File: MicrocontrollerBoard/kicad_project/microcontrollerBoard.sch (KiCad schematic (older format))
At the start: 48 parts, among them J1 PROG_CONN, J10 PC_5V, J13 PA_GND, J14 PB_GND, J15 PC_GND, J18 COM, J19 COM_5V, J2 5V_CONN, J20 COM_GND, J21 POWER_CONN, J22 MOTOR2, J23 MOTOR1, J3 PA, J4 PB, J5 PC, J6 3V_CONN_1, J7 3V_CONN_2, J8 PA_5V, J9 PB_5V, U1 ATmega1284P-PU, U2 TC4422, U3 TC4422, U4 TC4422, U5 TC4422, U6 AMS1117-3.3, Y1 16MHz

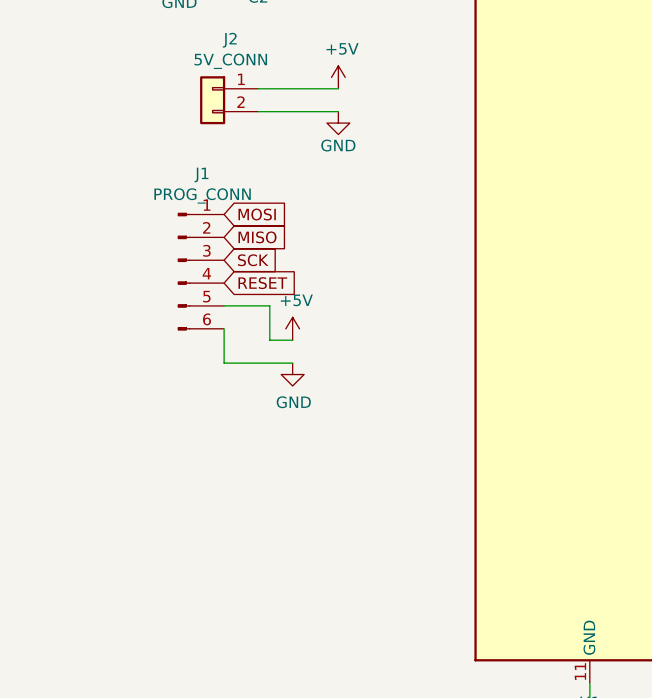
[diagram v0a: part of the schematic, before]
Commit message: uC board: Added resistors to MISO, brought out a RESET pin, minor fixes.
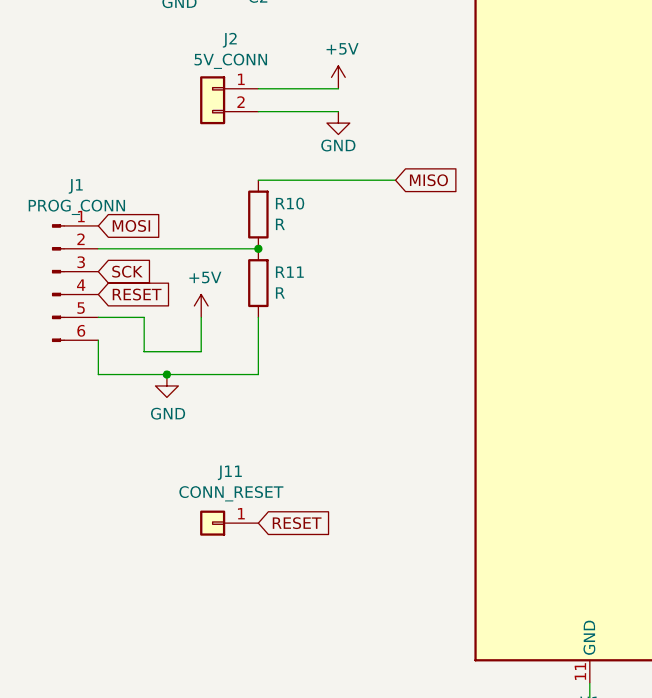
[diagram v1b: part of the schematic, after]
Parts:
- added J11: CONN_RESET, Connector_PinHeader_2.54mm:PinHeader_1x01_P2.54mm_Vertical, symbol Connector_Generic:Conn_01x01
- added R10, R11: R, Resistor_SMD:R_0805_2012Metric_Pad1.15x1.40mm_HandSolder, symbol Device:R
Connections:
- net GND: now also R11.1
- net MISO: now also R10.2; no longer J1.2 (Pin_2)
- net RESET: now also J11.1 (Pin_1)
- new net: J1.2 (Pin_2), R10.1, R11.2
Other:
- moved on the sheet: J1
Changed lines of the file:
@@
 L Connector:Conn_01x06_Male J1
 U 1 1 5BC7F9DC
-P 1500 3650
-F 0 "J1" H 1606 4028 50  0000 C CNN
-F 1 "PROG_CONN" H 1606 3937 50  0000 C CNN
-F 2 "Connector_PinHeader_2.54mm:PinHeader_1x06_P2.54mm_Vertical" H 1500 3650 50  0001 C CNN
-F 3 "~" H 1500 3650 50  0001 C CNN
-	1    1500 3650
+P 950 3700
+F 0 "J1" H 1056 4078 50  0000 C CNN
+F 1 "PROG_CONN" H 1056 3987 50  0000 C CNN
+F 2 "Connector_PinHeader_2.54mm:PinHeader_1x06_P2.54mm_Vertical" H 950 3700 50  0001 C CNN
+F 3 "~" H 950 3700 50  0001 C CNN
+	1    950  3700
 	1    0    0    -1
 $EndComp
@@
 L power:GND #PWR03
 U 1 1 5BC7FD8A
-P 2000 4100
-F 0 "#PWR03" H 2000 3850 50  0001 C CNN
-F 1 "GND" H 2005 3927 50  0000 C CNN
-F 2 "" H 2000 4100 50  0001 C CNN
-F 3 "" H 2000 4100 50  0001 C CNN
-	1    2000 4100
+P 1450 4150
+F 0 "#PWR03" H 1450 3900 50  0001 C CNN
+F 1 "GND" H 1455 3977 50  0000 C CNN
+F 2 "" H 1450 4150 50  0001 C CNN
+F 3 "" H 1450 4150 50  0001 C CNN
+	1    1450 4150
 	1    0    0    -1
 $EndComp
@@
 L power:+5V #PWR02
 U 1 1 5BC7FDAD
-P 2000 4000
-F 0 "#PWR02" H 2000 3850 50  0001 C CNN
-F 1 "+5V" H 2015 4173 50  0000 C CNN
-F 2 "" H 2000 4000 50  0001 C CNN
-F 3 "" H 2000 4000 50  0001 C CNN
-	1    2000 4000
-	1    0    0    -1
-$EndComp
-Text GLabel 1700 3750 2    50   Input ~ 0
+P 1600 3900
+F 0 "#PWR02" H 1600 3750 50  0001 C CNN
+F 1 "+5V" H 1615 4073 50  0000 C CNN
+F 2 "" H 1600 3900 50  0001 C CNN
+F 3 "" H 1600 3900 50  0001 C CNN
+	1    1600 3900
+	1    0    0    -1
+$EndComp
+Text GLabel 1150 3800 2    50   Input ~ 0
 RESET
-Text GLabel 1700 3650 2    50   Input ~ 0
+Text GLabel 1150 3700 2    50   Input ~ 0
 SCK
-Text GLabel 1700 3550 2    50   Input ~ 0
+Text GLabel 2450 3300 2    50   Input ~ 0
 MISO
-Text GLabel 1700 3450 2    50   Input ~ 0
+Text GLabel 1150 3500 2    50   Input ~ 0
 MOSI
 Wire Wire Line
-	1700 3850 1900 3850
-Wire Wire Line
-	1900 3850 1900 4000
-Wire Wire Line
-	1900 4000 2000 4000
-Wire Wire Line
-	1700 3950 1700 4100
-Wire Wire Line
-	1700 4100 2000 4100
+	1150 3900 1350 3900
+Wire Wire Line
+	1350 3900 1350 4050
+Wire Wire Line
+	1150 4000 1150 4150
+Wire Wire Line
+	1150 4150 1450 4150
 $Comp
 L Device:LED D1
@@
 	5800 6600 6300 6600
 Connection ~ 5800 6600
+$Comp
+L Connector_Generic:Conn_01x01 J11
+U 1 1 5BE3FF3A
+P 1650 4800
+F 0 "J11" H 1570 4575 50  0000 C CNN
+F 1 "CONN_RESET" H 1570 4666 50  0000 C CNN
+F 2 "Connector_PinHeader_2.54mm:PinHeader_1x01_P2.54mm_Vertical" H 1650 4800 50  0001 C CNN
+F 3 "~" H 1650 4800 50  0001 C CNN
+	1    1650 4800
+	-1   0    0    1
+$EndComp
+Text GLabel 1850 4800 2    50   Input ~ 0
+RESET
+$Comp
+L Device:R R10
+U 1 1 5BE4ABDC
+P 1850 3450
+F 0 "R10" H 1780 3404 50  0000 R CNN
+F 1 "R" H 1780 3495 50  0000 R CNN
+F 2 "Resistor_SMD:R_0805_2012Metric_Pad1.15x1.40mm_HandSolder" V 1780 3450 50  0001 C CNN
+F 3 "~" H 1850 3450 50  0001 C CNN
+	1    1850 3450
+	-1   0    0    1
+$EndComp
+$Comp
+L Device:R R11
+U 1 1 5BE4AE93
+P 1850 3750
+F 0 "R11" H 1780 3704 50  0000 R CNN
+F 1 "R" H 1780 3795 50  0000 R CNN
+F 2 "Resistor_SMD:R_0805_2012Metric_Pad1.15x1.40mm_HandSolder" V 1780 3750 50  0001 C CNN
+F 3 "~" H 1850 3750 50  0001 C CNN
+	1    1850 3750
+	-1   0    0    1
+$EndComp
+Wire Wire Line
+	1850 3600 1150 3600
+Connection ~ 1850 3600
+Wire Wire Line
+	1850 3900 1850 4150
+Wire Wire Line
+	1850 4150 1450 4150
+Connection ~ 1450 4150
+Wire Wire Line
+	1850 3300 2450 3300
+Wire Wire Line
+	1350 4050 1600 4050
+Wire Wire Line
+	1600 4050 1600 3900
 $EndSCHEMATC

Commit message: uC board: V_IN is no longer exposed. Better power routing.
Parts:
- J13, J3, J8: footprint Connector_PinHeader_2.54mm:PinHeader_1x08_P2.54mm_Vertical -> Connector_PinHeader_2.54mm:PinHeader_1x07_P2.54mm_Vertical; symbol Connector_Generic:Conn_01x08 -> Connector_Generic:Conn_01x07
- R10: value R -> 1K
- R11: value R -> 2K
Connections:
- net +5V: no longer J8.8 (Pin_8)
- net +BATT: now also R3.1
- net GND: no longer J13.8 (Pin_8)
- net at U1.33 (PA7): now also J3.7 (Pin_7); no longer J3.8 (Pin_8)
- net at U1.34 (PA6): now also J3.6 (Pin_6); no longer J3.7 (Pin_7)
- net at U1.35 (PA5): now also J3.5 (Pin_5); no longer J3.6 (Pin_6)
- net at U1.36 (PA4): now also J3.4 (Pin_4); no longer J3.5 (Pin_5)
- net at U1.37 (PA3): now also J3.3 (Pin_3); no longer J3.4 (Pin_4)
- net at U1.38 (PA2): now also J3.2 (Pin_2); no longer J3.3 (Pin_3)
- net at U1.39 (PA1): now also J3.1 (Pin_1); no longer J3.2 (Pin_2)
- removed net V_EXT: J3.1 (Pin_1), R3.1
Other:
- note added: "V_IN = V_BAT * R4 / ( R3 + R4)\n\nKeep V_IN < 5V with a safe margin!"
- note removed: "V_IN = V_EXT * RB / ( RA + RB)"
- moved on the sheet: R3, R4
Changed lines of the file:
@@
 L Device:R R3
 U 1 1 5BCE0BEC
-P 7150 1750
-F 0 "R3" H 7220 1796 50  0000 L CNN
-F 1 "RA" H 7220 1705 50  0000 L CNN
-F 2 "Resistor_SMD:R_0805_2012Metric_Pad1.15x1.40mm_HandSolder" V 7080 1750 50  0001 C CNN
-F 3 "~" H 7150 1750 50  0001 C CNN
-	1    7150 1750
+P 7000 2000
+F 0 "R3" H 7070 2046 50  0000 L CNN
+F 1 "RA" H 7070 1955 50  0000 L CNN
+F 2 "Resistor_SMD:R_0805_2012Metric_Pad1.15x1.40mm_HandSolder" V 6930 2000 50  0001 C CNN
+F 3 "~" H 7000 2000 50  0001 C CNN
+	1    7000 2000
 	1    0    0    -1
 $EndComp
@@
 L Device:R R4
 U 1 1 5BCE0BF2
-P 7150 2050
-F 0 "R4" H 7220 2096 50  0000 L CNN
-F 1 "RB" H 7220 2005 50  0000 L CNN
-F 2 "Resistor_SMD:R_0805_2012Metric_Pad1.15x1.40mm_HandSolder" V 7080 2050 50  0001 C CNN
-F 3 "~" H 7150 2050 50  0001 C CNN
-	1    7150 2050
+P 7000 2300
+F 0 "R4" H 7070 2346 50  0000 L CNN
+F 1 "RB" H 7070 2255 50  0000 L CNN
+F 2 "Resistor_SMD:R_0805_2012Metric_Pad1.15x1.40mm_HandSolder" V 6930 2300 50  0001 C CNN
+F 3 "~" H 7000 2300 50  0001 C CNN
+	1    7000 2300
 	1    0    0    -1
 $EndComp
@@
 L power:GND #PWR015
 U 1 1 5BCE0BF8
-P 7150 2200
-F 0 "#PWR015" H 7150 1950 50  0001 C CNN
-F 1 "GND" H 7155 2027 50  0000 C CNN
-F 2 "" H 7150 2200 50  0001 C CNN
-F 3 "" H 7150 2200 50  0001 C CNN
-	1    7150 2200
-	1    0    0    -1
-$EndComp
-Text GLabel 7450 1600 2    50   Input ~ 0
-V_EXT
-Wire Wire Line
-	7150 1600 7450 1600
-Wire Wire Line
-	7150 1900 6850 1900
-Connection ~ 7150 1900
-Text GLabel 6850 1900 0    50   Input ~ 0
+P 7000 2450
+F 0 "#PWR015" H 7000 2200 50  0001 C CNN
+F 1 "GND" H 7005 2277 50  0000 C CNN
+F 2 "" H 7000 2450 50  0001 C CNN
+F 3 "" H 7000 2450 50  0001 C CNN
+	1    7000 2450
+	1    0    0    -1
+$EndComp
+Wire Wire Line
+	7000 1850 7300 1850
+Wire Wire Line
+	7000 2150 6700 2150
+Connection ~ 7000 2150
+Text GLabel 6700 2150 0    50   Input ~ 0
 V_IN
-Text GLabel 3900 1800 2    50   Input ~ 0
-V_IN
-Text Notes 6600 2500 0    50   ~ 0
-V_IN = V_EXT * RB / ( RA + RB)
+Text Notes 6450 3000 0    50   ~ 0
+  V_IN = V_BAT * R4 / ( R3 + R4)\n\nKeep V_IN < 5V with a safe margin!
 $Comp
 L Connector_Generic:Conn_01x04 J9
@@
 $EndComp
 $Comp
-L Connector_Generic:Conn_01x08 J3
+L Connector_Generic:Conn_01x07 J3
 U 1 1 5BD3F1C1
-P 4800 2100
-F 0 "J3" H 4750 2600 50  0000 L CNN
-F 1 "PA" H 4750 2500 50  0000 L CNN
-F 2 "Connector_PinHeader_2.54mm:PinHeader_1x08_P2.54mm_Vertical" H 4800 2100 50  0001 C CNN
-F 3 "~" H 4800 2100 50  0001 C CNN
-	1    4800 2100
+P 4800 2200
+F 0 "J3" H 4750 2700 50  0000 L CNN
+F 1 "PA" H 4750 2600 50  0000 L CNN
+F 2 "Connector_PinHeader_2.54mm:PinHeader_1x07_P2.54mm_Vertical" H 4800 2200 50  0001 C CNN
+F 3 "~" H 4800 2200 50  0001 C CNN
+	1    4800 2200
 	1    0    0    -1
 $EndComp
@@
 Wire Wire Line
 	4600 1900 3900 1900
-Text GLabel 4600 1800 0    50   Input ~ 0
-V_EXT
-$Comp
-L Connector_Generic:Conn_01x08 J8
+$Comp
+L Connector_Generic:Conn_01x07 J8
 U 1 1 5BD6F2E7
-P 5350 2100
-F 0 "J8" H 5300 2600 50  0000 L CNN
-F 1 "PA_5V" H 5300 2500 50  0000 L CNN
-F 2 "Connector_PinHeader_2.54mm:PinHeader_1x08_P2.54mm_Vertical" H 5350 2100 50  0001 C CNN
-F 3 "~" H 5350 2100 50  0001 C CNN
-	1    5350 2100
-	1    0    0    -1
-$EndComp
-$Comp
-L Connector_Generic:Conn_01x08 J13
+P 5350 2200
+F 0 "J8" H 5300 2700 50  0000 L CNN
+F 1 "PA_5V" H 5300 2600 50  0000 L CNN
+F 2 "Connector_PinHeader_2.54mm:PinHeader_1x07_P2.54mm_Vertical" H 5350 2200 50  0001 C CNN
+F 3 "~" H 5350 2200 50  0001 C CNN
+	1    5350 2200
+	1    0    0    -1
+$EndComp
+$Comp
+L Connector_Generic:Conn_01x07 J13
 U 1 1 5BD6F3CA
-P 5900 2100
-F 0 "J13" H 5850 2600 50  0000 L CNN
-F 1 "PA_GND" H 5850 2500 50  0000 L CNN
-F 2 "Connector_PinHeader_2.54mm:PinHeader_1x08_P2.54mm_Vertical" H 5900 2100 50  0001 C CNN
-F 3 "~" H 5900 2100 50  0001 C CNN
-	1    5900 2100
-	1    0    0    -1
-$EndComp
-Wire Wire Line
-	5150 2800 5150 2500
-Wire Wire Line
-	5150 2500 5150 2400
-Connection ~ 5150 2500
-Wire Wire Line
-	5150 2400 5150 2300
-Connection ~ 5150 2400
-Wire Wire Line
-	5150 2300 5150 2200
-Connection ~ 5150 2300
-Wire Wire Line
-	5150 2200 5150 2100
-Connection ~ 5150 2200
-Wire Wire Line
-	5150 2100 5150 2000
-Connection ~ 5150 2100
-Wire Wire Line
-	5150 2000 5150 1900
-Connection ~ 5150 2000
-Wire Wire Line
-	5150 1900 5150 1800
-Connection ~ 5150 1900
-Wire Wire Line
-	5700 2800 5700 2500
+P 5900 2200
+F 0 "J13" H 5850 2700 50  0000 L CNN
+F 1 "PA_GND" H 5850 2600 50  0000 L CNN
+F 2 "Connector_PinHeader_2.54mm:PinHeader_1x07_P2.54mm_Vertical" H 5900 2200 50  0001 C CNN
+F 3 "~" H 5900 2200 50  0001 C CNN
+	1    5900 2200
+	1    0    0    -1
+$EndComp
 Connection ~ 5700 2800
-Wire Wire Line
-	5700 2500 5700 2400
-Connection ~ 5700 2500
-Wire Wire Line
-	5700 2400 5700 2300
-Connection ~ 5700 2400
-Wire Wire Line
-	5700 2300 5700 2200
-Connection ~ 5700 2300
-Wire Wire Line
-	5700 2200 5700 2100
-Connection ~ 5700 2200
-Wire Wire Line
-	5700 2100 5700 2000
-Connection ~ 5700 2100
-Wire Wire Line
-	5700 2000 5700 1900
-Connection ~ 5700 2000
-Wire Wire Line
-	5700 1900 5700 1800
-Connection ~ 5700 1900
 $Comp
 L Connector_Generic:Conn_01x04 J18
@@
 	1    0    0    -1
 $EndComp
-Wire Wire Line
-	5150 1650 5150 1800
-Connection ~ 5150 1800
 $Comp
 L Connector_Generic:Conn_01x08 J15
@@
 P 1850 3450
 F 0 "R10" H 1780 3404 50  0000 R CNN
-F 1 "R" H 1780 3495 50  0000 R CNN
+F 1 "1K" H 1780 3495 50  0000 R CNN
 F 2 "Resistor_SMD:R_0805_2012Metric_Pad1.15x1.40mm_HandSolder" V 1780 3450 50  0001 C CNN
 F 3 "~" H 1850 3450 50  0001 C CNN
@@
 P 1850 3750
 F 0 "R11" H 1780 3704 50  0000 R CNN
-F 1 "R" H 1780 3795 50  0000 R CNN
+F 1 "2K" H 1780 3795 50  0000 R CNN
 F 2 "Resistor_SMD:R_0805_2012Metric_Pad1.15x1.40mm_HandSolder" V 1780 3750 50  0001 C CNN
 F 3 "~" H 1850 3750 50  0001 C CNN
@@
 Wire Wire Line
 	1600 4050 1600 3900
+Connection ~ 5150 1900
+Connection ~ 5150 2000
+Connection ~ 5150 2100
+Connection ~ 5150 2200
+Connection ~ 5150 2300
+Connection ~ 5150 2400
+Connection ~ 5150 2500
+Wire Wire Line
+	5150 2500 5150 2800
+Wire Wire Line
+	5150 2400 5150 2500
+Wire Wire Line
+	5150 1650 5150 1900
+Wire Wire Line
+	5150 2300 5150 2400
+Wire Wire Line
+	5150 2200 5150 2300
+Wire Wire Line
+	5150 2100 5150 2200
+Wire Wire Line
+	5150 2000 5150 2100
+Wire Wire Line
+	5150 1900 5150 2000
+Wire Wire Line
+	5700 1900 5700 2000
+Wire Wire Line
+	5700 2000 5700 2100
+Connection ~ 5700 2000
+Wire Wire Line
+	5700 2100 5700 2200
+Connection ~ 5700 2100
+Wire Wire Line
+	5700 2200 5700 2300
+Connection ~ 5700 2200
+Wire Wire Line
+	5700 2300 5700 2400
+Connection ~ 5700 2300
+Wire Wire Line
+	5700 2400 5700 2500
+Connection ~ 5700 2400
+Wire Wire Line
+	5700 2500 5700 2800
+Connection ~ 5700 2500
+$Comp
+L power:+BATT #PWR0101
+U 1 1 5BEFB538
+P 7300 1850
+F 0 "#PWR0101" H 7300 1700 50  0001 C CNN
+F 1 "+BATT" H 7315 2023 50  0000 C CNN
+F 2 "" H 7300 1850 50  0001 C CNN
+F 3 "" H 7300 1850 50  0001 C CNN
+	1    7300 1850
+	1    0    0    -1
+$EndComp
+Text GLabel 3900 1800 2    50   Input ~ 0
+V_IN
 $EndSCHEMATC

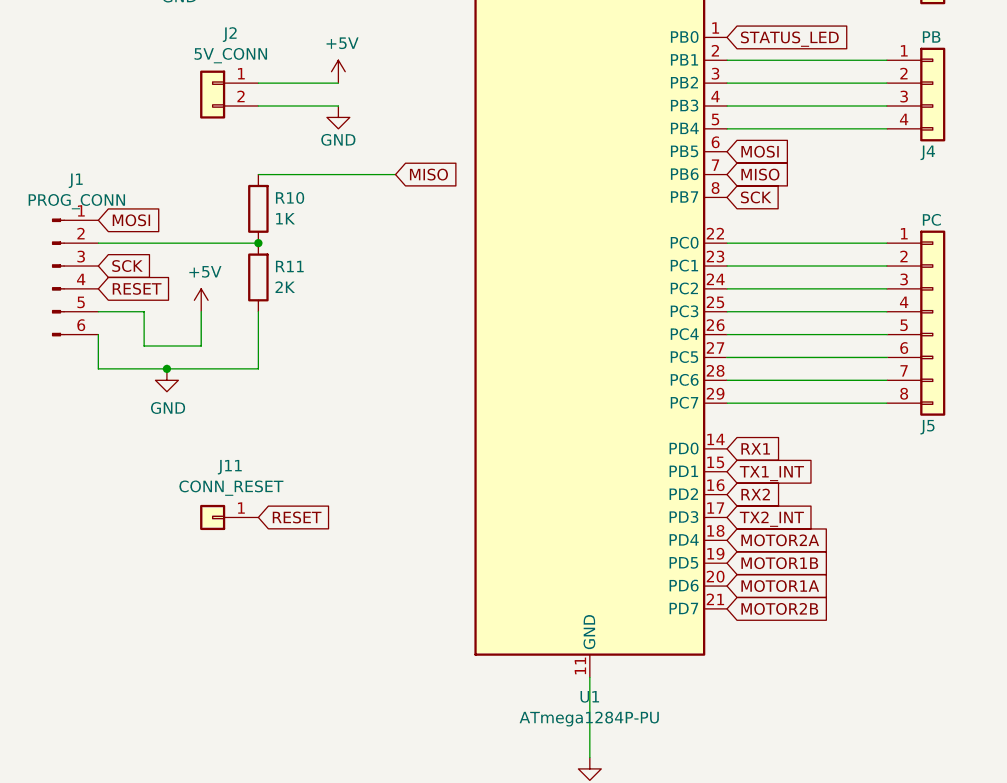
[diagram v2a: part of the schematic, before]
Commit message: Revised ICSP header, motor diodes.
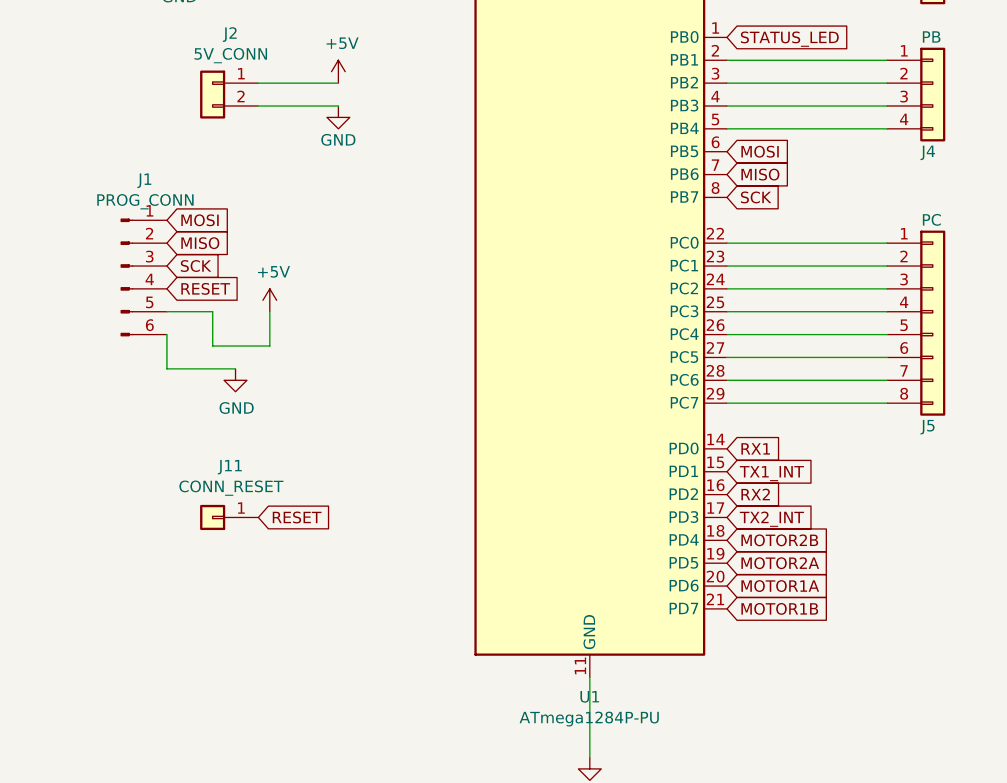
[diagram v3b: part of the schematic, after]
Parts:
- removed R10: 1K, Resistor_SMD:R_0805_2012Metric_Pad1.15x1.40mm_HandSolder, symbol Device:R
- removed R11: 2K, Resistor_SMD:R_0805_2012Metric_Pad1.15x1.40mm_HandSolder, symbol Device:R
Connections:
- net MISO: now also J1.2 (Pin_2)
- net MOTOR1B: now also U1.21 (PD7); no longer U1.19 (PD5)
- net MOTOR2A: now also U1.19 (PD5); no longer U1.18 (PD4)
- net MOTOR2B: now also U1.18 (PD4); no longer U1.21 (PD7)
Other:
- moved on the sheet: J1
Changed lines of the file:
@@
 L Connector:Conn_01x06_Male J1
 U 1 1 5BC7F9DC
-P 950 3700
-F 0 "J1" H 1056 4078 50  0000 C CNN
-F 1 "PROG_CONN" H 1056 3987 50  0000 C CNN
-F 2 "Connector_PinHeader_2.54mm:PinHeader_1x06_P2.54mm_Vertical" H 950 3700 50  0001 C CNN
-F 3 "~" H 950 3700 50  0001 C CNN
-	1    950  3700
+P 1250 3700
+F 0 "J1" H 1356 4078 50  0000 C CNN
+F 1 "PROG_CONN" H 1356 3987 50  0000 C CNN
+F 2 "Connector_PinHeader_2.54mm:PinHeader_1x06_P2.54mm_Vertical" H 1250 3700 50  0001 C CNN
+F 3 "~" H 1250 3700 50  0001 C CNN
+	1    1250 3700
 	1    0    0    -1
 $EndComp
@@
 L power:GND #PWR03
 U 1 1 5BC7FD8A
-P 1450 4150
-F 0 "#PWR03" H 1450 3900 50  0001 C CNN
-F 1 "GND" H 1455 3977 50  0000 C CNN
-F 2 "" H 1450 4150 50  0001 C CNN
-F 3 "" H 1450 4150 50  0001 C CNN
-	1    1450 4150
+P 1750 4150
+F 0 "#PWR03" H 1750 3900 50  0001 C CNN
+F 1 "GND" H 1755 3977 50  0000 C CNN
+F 2 "" H 1750 4150 50  0001 C CNN
+F 3 "" H 1750 4150 50  0001 C CNN
+	1    1750 4150
 	1    0    0    -1
 $EndComp
@@
 L power:+5V #PWR02
 U 1 1 5BC7FDAD
-P 1600 3900
-F 0 "#PWR02" H 1600 3750 50  0001 C CNN
-F 1 "+5V" H 1615 4073 50  0000 C CNN
-F 2 "" H 1600 3900 50  0001 C CNN
-F 3 "" H 1600 3900 50  0001 C CNN
-	1    1600 3900
-	1    0    0    -1
-$EndComp
-Text GLabel 1150 3800 2    50   Input ~ 0
+P 1900 3900
+F 0 "#PWR02" H 1900 3750 50  0001 C CNN
+F 1 "+5V" H 1915 4073 50  0000 C CNN
+F 2 "" H 1900 3900 50  0001 C CNN
+F 3 "" H 1900 3900 50  0001 C CNN
+	1    1900 3900
+	1    0    0    -1
+$EndComp
+Text GLabel 1450 3800 2    50   Input ~ 0
 RESET
-Text GLabel 1150 3700 2    50   Input ~ 0
+Text GLabel 1450 3700 2    50   Input ~ 0
 SCK
-Text GLabel 2450 3300 2    50   Input ~ 0
+Text GLabel 1450 3600 2    50   Input ~ 0
 MISO
-Text GLabel 1150 3500 2    50   Input ~ 0
+Text GLabel 1450 3500 2    50   Input ~ 0
 MOSI
 Wire Wire Line
-	1150 3900 1350 3900
-Wire Wire Line
-	1350 3900 1350 4050
-Wire Wire Line
-	1150 4000 1150 4150
-Wire Wire Line
-	1150 4150 1450 4150
+	1450 3900 1650 3900
+Wire Wire Line
+	1650 3900 1650 4050
+Wire Wire Line
+	1450 4000 1450 4150
+Wire Wire Line
+	1450 4150 1750 4150
 $Comp
 L Device:LED D1
@@
 Text GLabel 3900 5100 2    50   Input ~ 0
 MOTOR1A
+Text GLabel 3900 5200 2    50   Input ~ 0
+MOTOR1B
 Text GLabel 3900 5000 2    50   Input ~ 0
-MOTOR1B
+MOTOR2A
 Text GLabel 3900 4900 2    50   Input ~ 0
-MOTOR2A
-Text GLabel 3900 5200 2    50   Input ~ 0
 MOTOR2B
 Wire Wire Line
@@
 Text GLabel 1850 4800 2    50   Input ~ 0
 RESET
-$Comp
-L Device:R R10
-U 1 1 5BE4ABDC
-P 1850 3450
-F 0 "R10" H 1780 3404 50  0000 R CNN
-F 1 "1K" H 1780 3495 50  0000 R CNN
-F 2 "Resistor_SMD:R_0805_2012Metric_Pad1.15x1.40mm_HandSolder" V 1780 3450 50  0001 C CNN
-F 3 "~" H 1850 3450 50  0001 C CNN
-	1    1850 3450
-	-1   0    0    1
-$EndComp
-$Comp
-L Device:R R11
-U 1 1 5BE4AE93
-P 1850 3750
-F 0 "R11" H 1780 3704 50  0000 R CNN
-F 1 "2K" H 1780 3795 50  0000 R CNN
-F 2 "Resistor_SMD:R_0805_2012Metric_Pad1.15x1.40mm_HandSolder" V 1780 3750 50  0001 C CNN
-F 3 "~" H 1850 3750 50  0001 C CNN
-	1    1850 3750
-	-1   0    0    1
-$EndComp
-Wire Wire Line
-	1850 3600 1150 3600
-Connection ~ 1850 3600
-Wire Wire Line
-	1850 3900 1850 4150
-Wire Wire Line
-	1850 4150 1450 4150
-Connection ~ 1450 4150
-Wire Wire Line
-	1850 3300 2450 3300
-Wire Wire Line
-	1350 4050 1600 4050
-Wire Wire Line
-	1600 4050 1600 3900
+Wire Wire Line
+	1650 4050 1900 4050
+Wire Wire Line
+	1900 4050 1900 3900
 Connection ~ 5150 1900
 Connection ~ 5150 2000
